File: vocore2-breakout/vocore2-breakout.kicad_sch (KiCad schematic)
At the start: 20 parts, among them J1 Conn_01x16_Socket, J2 Conn_01x12_Socket, J3 Conn_01x14_Socket, J4 Conn_01x15_Socket, J5 Conn_02x06_Odd_Even, J6 Conn_02x05_Odd_Even, U1 VOCORE2-SMT

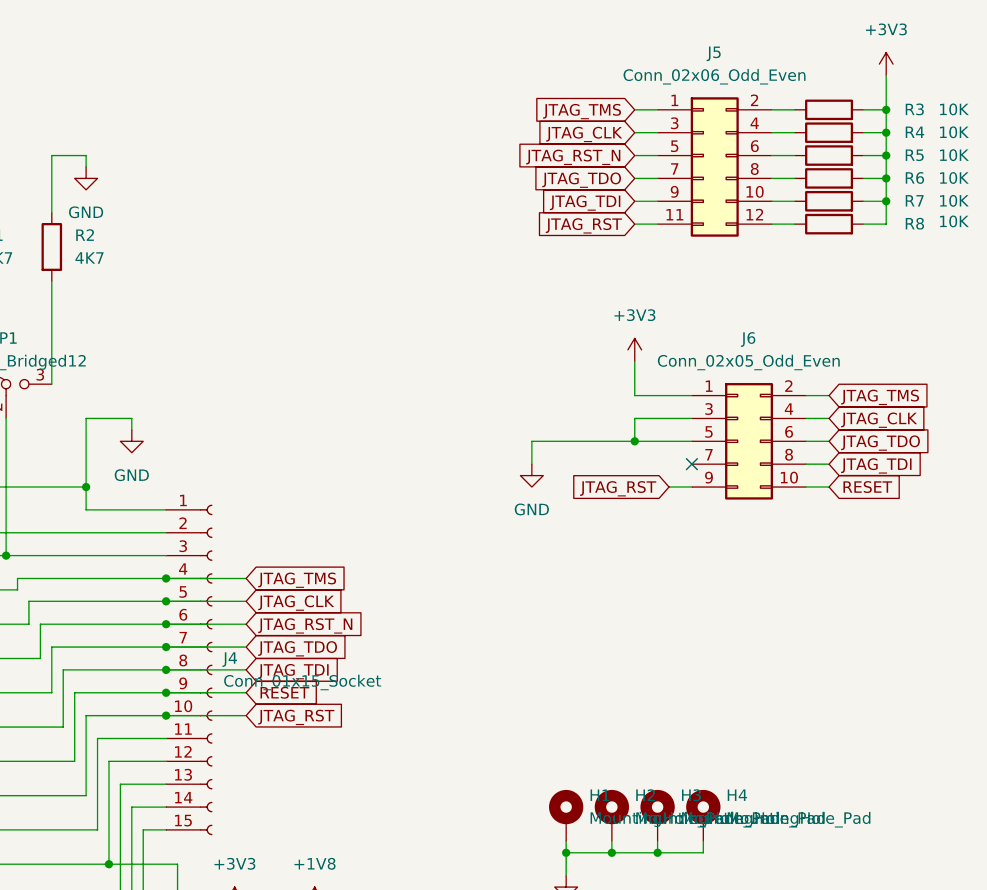
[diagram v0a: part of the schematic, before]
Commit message: Use correct jtag reset
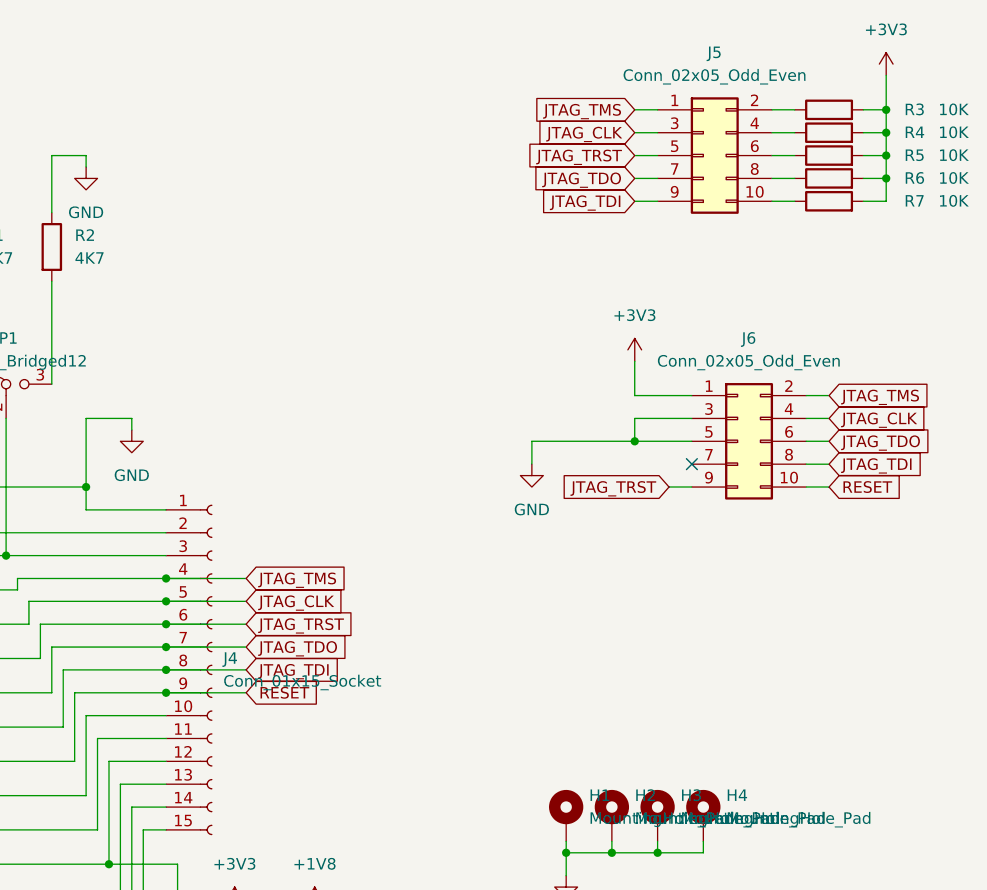
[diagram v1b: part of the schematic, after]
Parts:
- removed J5: Conn_02x06_Odd_Even, Connector_PinHeader_2.54mm:PinHeader_2x06_P2.54mm_Vertical, symbol Connector_Generic:Conn_02x06_Odd_Even
- removed R8: 10K, Resistor_SMD:R_0805_2012Metric_Pad1.20x1.40mm_HandSolder, symbol Device:R
- added J5: Conn_02x05_Odd_Even, Connector_PinHeader_2.54mm:PinHeader_2x05_P2.54mm_Vertical, symbol Connector_Generic:Conn_02x05_Odd_Even
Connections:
- net JTAG_CLK: now also J5.3 (Pin_3)
- net JTAG_TDI: now also J5.9 (Pin_9)
- net JTAG_TDO: now also J5.7 (Pin_7)
- net JTAG_TMS: now also J5.1 (Pin_1)
- net at R4.1: now also J5.4 (Pin_4)
- net at R7.1: now also J5.10 (Pin_10)
- net at R3.1: now also J5.2 (Pin_2)
- net at R5.1: now also J5.6 (Pin_6)
- net at R6.1: now also J5.8 (Pin_8)
- net JTAG_RST: no longer names the net of J4.10 (Pin_10), U1.R10 (GPIO38)
- net JTAG_RST: no longer J6.9 (Pin_9)
- net JTAG_RST_N renamed JTAG_TRST
- net JTAG_TRST: now also J6.9 (Pin_9), J5.5 (Pin_5)
